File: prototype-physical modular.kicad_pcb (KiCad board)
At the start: 2 copper layers, 100 x 164 mm, 187 parts, among them CON1 BARREL_JACK, CON2 SD_Card_SEEEDOPL, IC1 ATMEGA2560-A, P1 POWER, P10 PC, P11 CONN_UART, P12 PJ, P13 PD, P14 PE, P15 PH, P16 PF, P17 SD_PINS, P18 3VI2C, P19 PIGPIO, P2 FTDI, P20 MIDI_IN, P21 MIDI_OUT, P22 BUSTI, P23 BUSTO, P3 SPI, P7 PA, P8 PL, P9 PB, Q1 BSS138, Q2 BSS138, Q3 BSS138, Q4 BSS138, Q5 BSS138, Q6 BSS138, SW1 SW_PUSH, SW10 SW_PUSH, SW11 SW_PUSH, SW12 SW_PUSH, SW13 SW_PUSH, SW14 SW_PUSH, SW2 ROTARY_ENCODER_SWITCH, SW3 SW_PUSH, SW4 SW_PUSH, SW5 SW_PUSH, SW6 SW_PUSH, SW7 SW_PUSH, SW8 SW_PUSH, SW9 SW_PUSH, U1 NCP1117ST50T3G, U2 6N138, Y1 16MHz

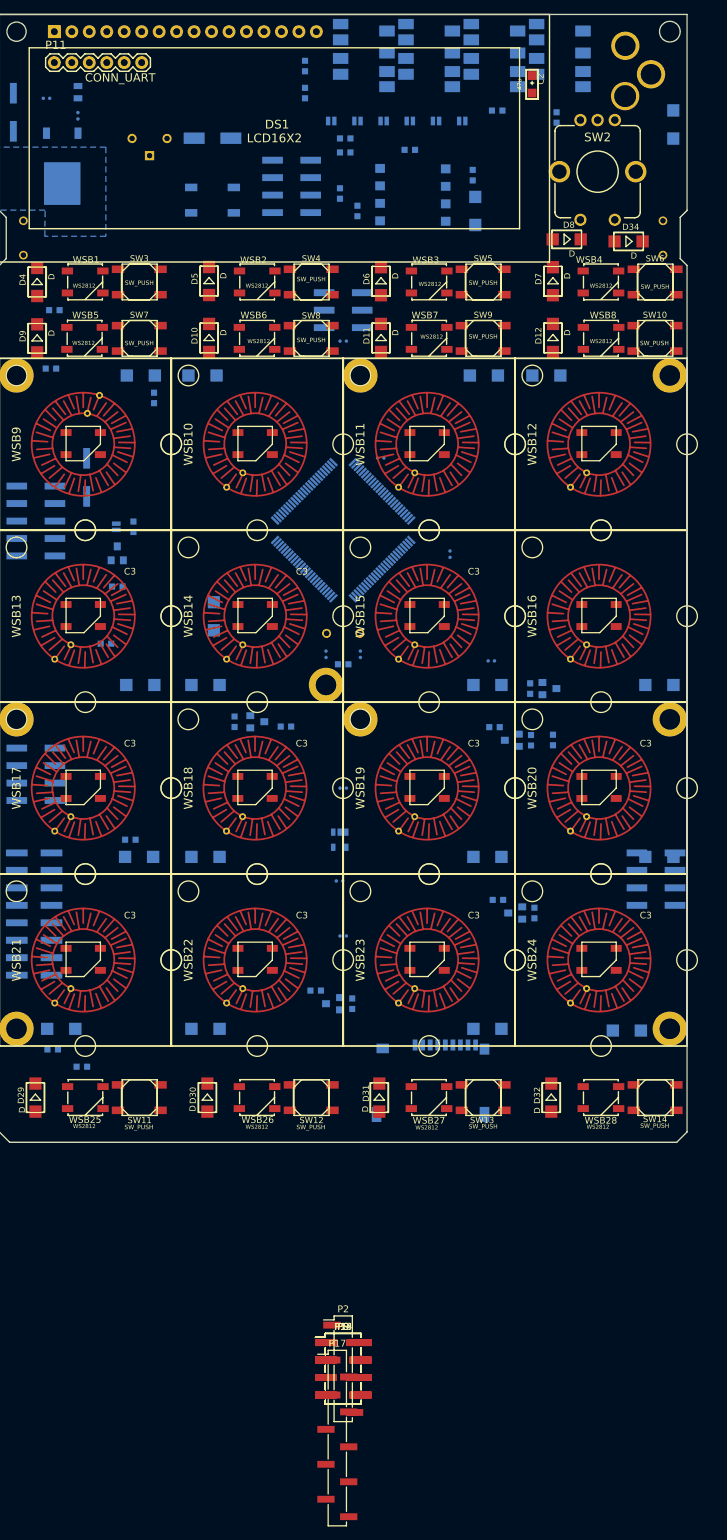
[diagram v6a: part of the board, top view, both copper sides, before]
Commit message: flip FTDI to correct side, draw size fro better fit with enclosure & many others
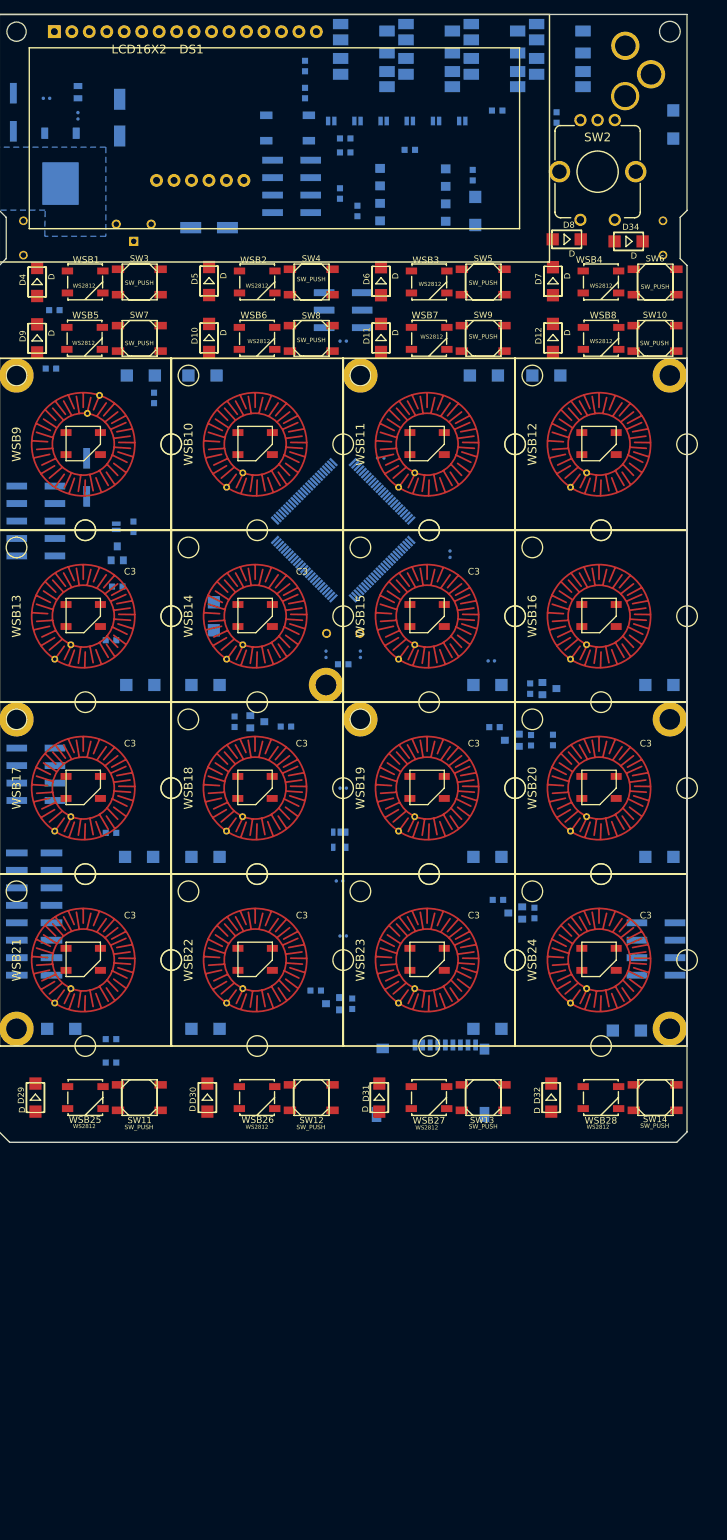
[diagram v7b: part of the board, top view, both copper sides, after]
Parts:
- removed P13: PD, Pin_Headers:Pin_Header_Straight_2x04_Pitch2.54mm_SMD
- removed P14: PE, Pin_Headers:Pin_Header_Straight_2x04_Pitch2.54mm_SMD
- removed P17: SD_PINS, Pin_Headers:Pin_Header_Straight_1x10_Pitch2.54mm_SMD_Pin1Left
- removed P2: FTDI, Pin_Headers:Pin_Header_Straight_1x06_Pitch2.54mm_SMD_Pin1Left
- removed P8: PL, Pin_Headers:Pin_Header_Straight_2x04_Pitch2.54mm_SMD
- removed P9: PB, Pin_Headers:Pin_Header_Straight_2x04_Pitch2.54mm_SMD
- C2: value 47u -> Aluminum 47uF-25V; footprint lib_fp:AVX-A -> SeeedOPL-Capacitor:ELECTRO-SMD-C-6MM; moved to B.Cu
- P11: moved to B.Cu
- moved C2 60.2 mm to (17.5, 15.0), turned to 90 degrees
- moved P11 32.4 mm to (35.6, 24.1), turned to 180 degrees
- moved SW1 15.1 mm to (41.9, 16.5)
- moved C11 13.0 mm to (30.5, 31.0)
- moved RV1 12.7 mm to (19.5, 33.0)
- moved P15 10.2 mm to (95.5, 135.9)
- moved R30 8.61 mm to (16.2, 149.0)
- moved R31 4.28 mm to (16.2, 152.4)
- moved R29 2.98 mm to (16.2, 119.0)
- moved R28 0.89 mm to (16.2, 91.0)
- moved U1 0.25 mm to (8.89, 22.1)
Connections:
- net /SD_CD renamed /SD_CDetc
- C2 pad +: Net-(C1-Pad1) -> GND
- C2 pad -: GND -> Net-(C1-Pad1)
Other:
- net class Default: clearance 0.2 -> 0.2032; trace_width 0.25 -> 0.2032
- rule trace_clearance: 0.2 -> 0.2032

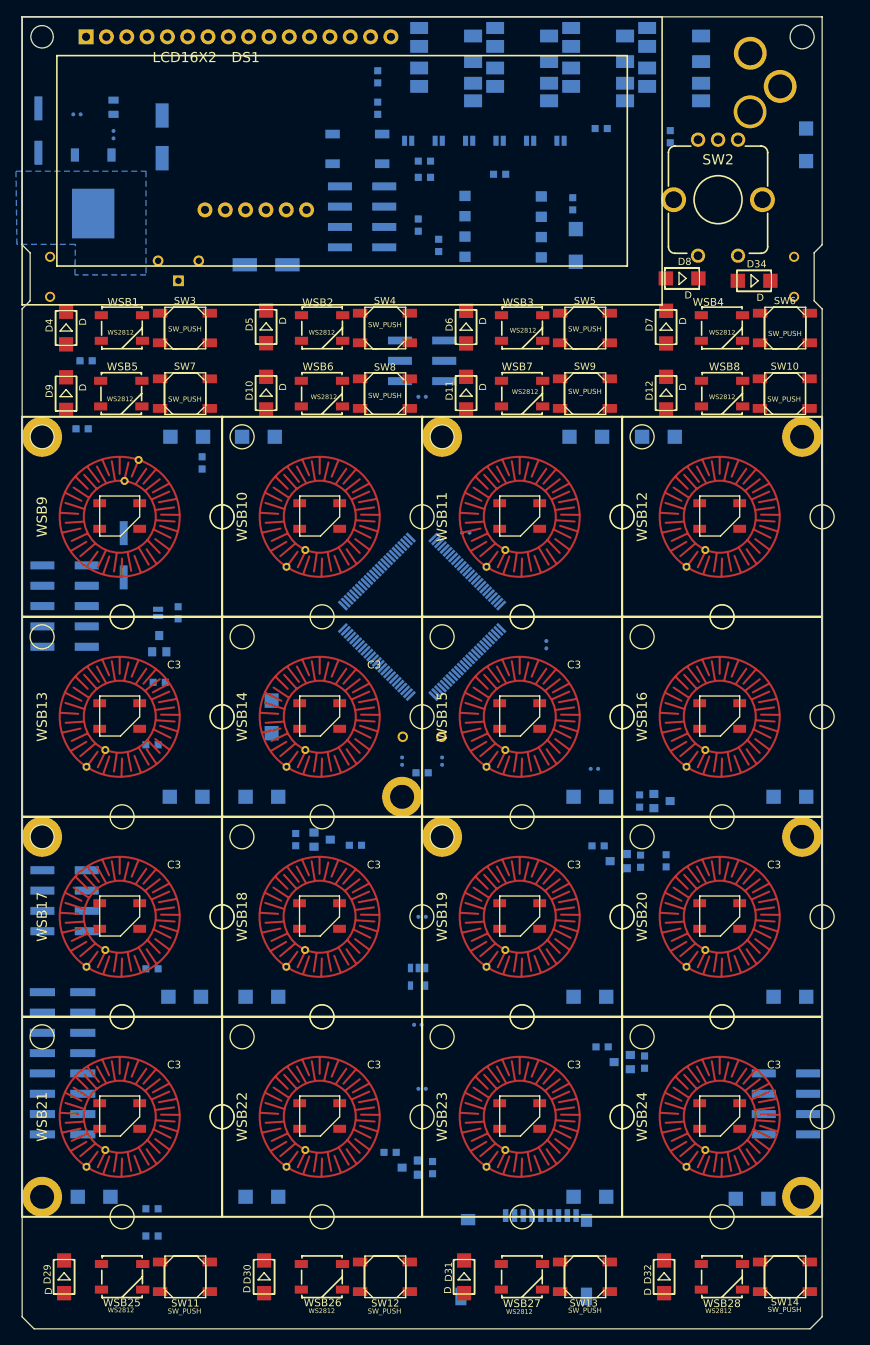
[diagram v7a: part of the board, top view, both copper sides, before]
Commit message: select better tact switches, add holes in the schematic to avoid future problems
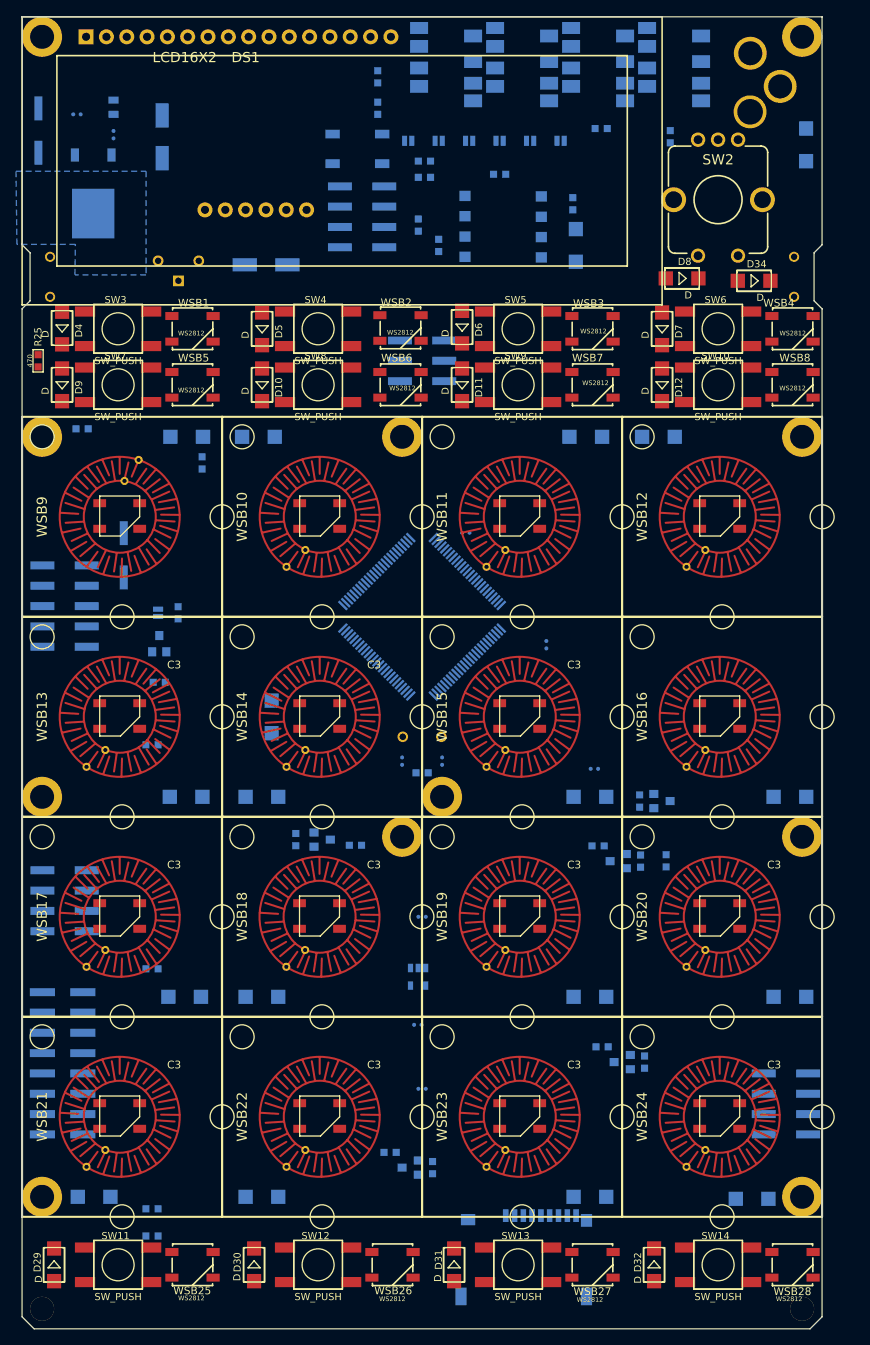
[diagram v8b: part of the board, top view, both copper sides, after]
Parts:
- removed REF00, REF01, REF02, REF03, REF04, REF05, REF06, REF07, REF08, REF09, REF10, REF11, REF12, REF13, REF15, REF16, REF17, REF18, REF19, REF20, REF21, REF22, REF23, REF28: MountingHole_3mm, lib_fp:MountingHole_3mm
- added H1: hole, lib_fp:hole_no-copper, F.Cu at (75.0, 137.5)
- added H10: hole, lib_fp:hole_no-copper, F.Cu at (25.0, 112.5)
- added H11: hole, lib_fp:hole_no-copper, F.Cu at (12.5, 125.0)
- added H12: hole, lib_fp:hole_no-copper, F.Cu at (75.0, 87.5)
- added H14: hole, lib_fp:hole_with-copper, F.Cu at (47.5, 52.5)
- added H15: hole, lib_fp:hole_with-copper, F.Cu at (97.5, 52.5)
- added H16: hole, lib_fp:hole_with-copper, F.Cu at (52.5, 97.5)
- added H18: hole, lib_fp:hole_with-copper, F.Cu at (47.5, 102.5)
- added H2: hole, lib_fp:hole_no-copper, F.Cu at (12.5, 75.0)
- added H20: hole, lib_fp:hole_with-copper, F.Cu at (97.5, 2.50)
- added H21: hole, lib_fp:hole_with-copper, F.Cu at (97.5, 102.5)
- added H22: hole, lib_fp:hole_with-copper, F.Cu at (2.50, 97.5)
- added H23: hole, lib_fp:hole_with-copper, F.Cu at (2.50, 147.5)
- added H24: hole, lib_fp:hole_with-copper, F.Cu at (97.5, 147.5)
- added H26: hole, lib_fp:hole_no-copper, F.Cu at (97.5, 161.5)
- added H27: hole, lib_fp:hole_no-copper, F.Cu at (87.5, 125.0)
- added H28: hole, lib_fp:hole_no-copper, F.Cu at (2.50, 161.5)
- added H29: hole, lib_fp:hole_no-copper, F.Cu at (75.0, 112.5)
- added H3: hole, lib_fp:hole_no-copper, F.Cu at (87.5, 75.0)
- added H30: hole, lib_fp:hole_no-copper, F.Cu at (62.5, 125.0)
- added H4: hole, lib_fp:hole_no-copper, F.Cu at (25.0, 62.5)
- added H5: hole, lib_fp:hole_no-copper, F.Cu at (62.5, 75.0)
- added H6: hole, lib_fp:hole_no-copper, F.Cu at (25.0, 87.5)
- added H7: hole, lib_fp:hole_no-copper, F.Cu at (25.0, 137.5)
- added H8: hole, lib_fp:hole_no-copper, F.Cu at (37.5, 125.0)
- added H9: hole, lib_fp:hole_no-copper, F.Cu at (75.0, 62.5)
- IC1: footprint SeeedOPL-IC:TQFP100-0.5-14X14MM -> SparkFun-DigitalIC:TQFP100
- R25: moved to F.Cu
- SW10, SW11, SW12, SW13, SW14, SW3, SW4, SW5, SW6, SW7, SW8, SW9: footprint lib_fp:SW4-SMD-5.2X5.2X1.5MM -> lib_fp:SW4-SMD-6.0X6.0X5.0MM
- moved WSB6 9.88 mm to (47.3, 46.0)
- moved WSB2 9.80 mm to (47.3, 38.9)
- moved WSB5 8.97 mm to (21.3, 46.0)
- moved WSB26 8.95 mm to (46.3, 156.0)
- moved WSB27 8.95 mm to (71.3, 156.0)
- moved WSB28 8.95 mm to (96.3, 156.0)
- moved WSB25 8.93 mm to (21.3, 156.0)
- moved WSB7 8.87 mm to (71.3, 46.0)
- moved WSB8 8.87 mm to (96.3, 46.0)
- moved WSB1 8.82 mm to (21.3, 39.0)
- moved WSB4 8.82 mm to (96.3, 39.0)
- moved WSB3 8.80 mm to (71.3, 39.0)
- moved SW11 8.49 mm to (12.0, 156.0)
- moved SW12 8.49 mm to (37.0, 156.0)
- moved SW13 8.49 mm to (62.0, 156.0)
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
